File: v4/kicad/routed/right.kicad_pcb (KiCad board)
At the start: 2 copper layers, 158 x 118.6 mm, 72 parts

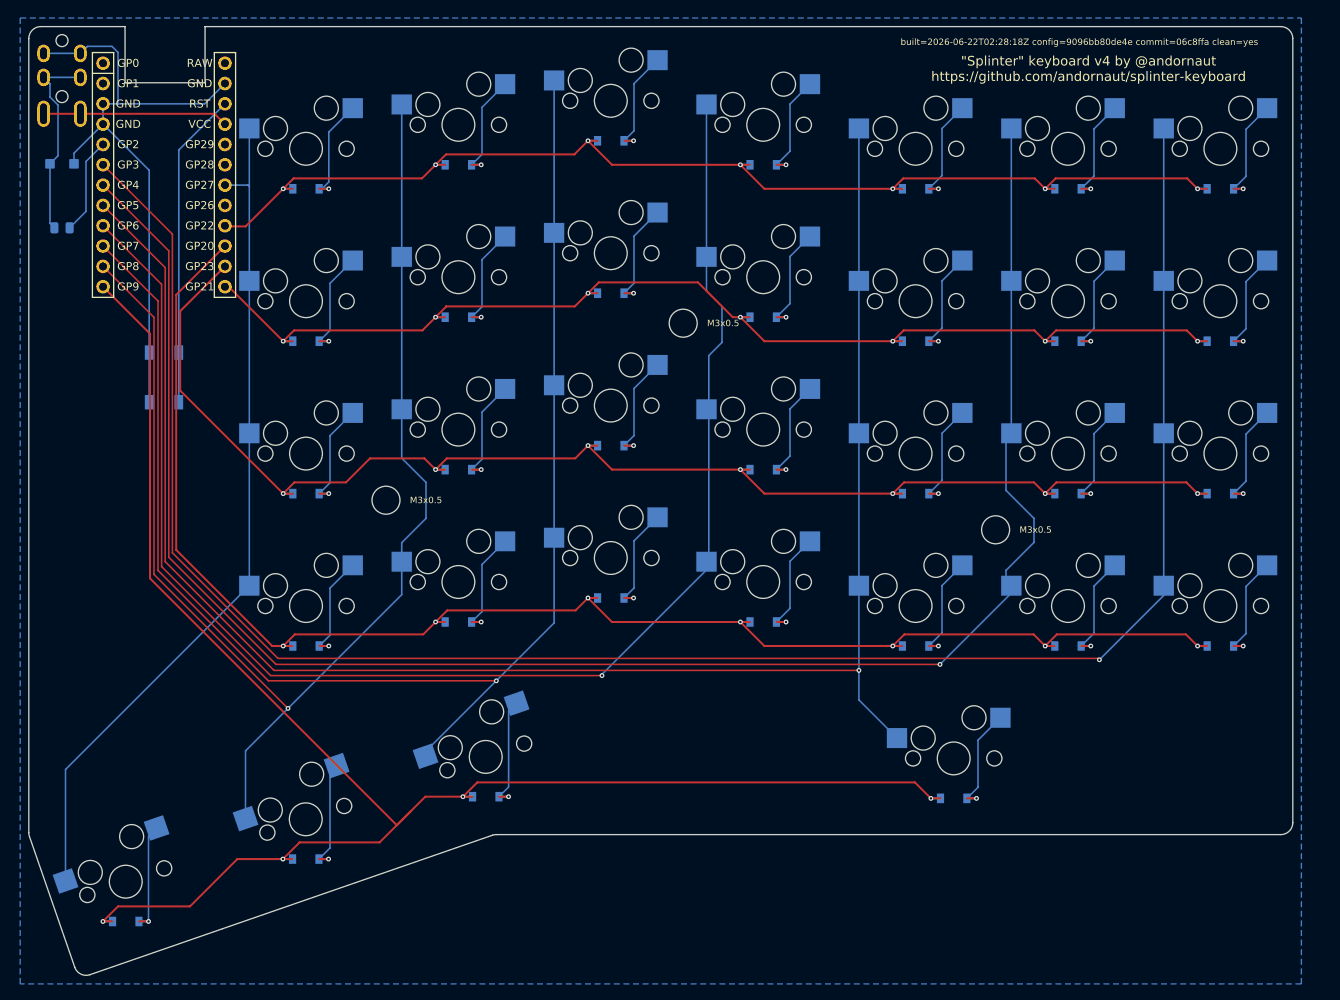
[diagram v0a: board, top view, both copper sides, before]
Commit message: v4: re-route both halves for the mirrored left-half pin mapping
Both halves are routed against the current config: the left half's matrix
nets on their MCU socket-row partners, and the MCU seated at the new mcu_y.
routed/ is re-derived from unrouted/ with the GND pour and teardrops (281
left, 296 right).

validate:provenance, validate:firmware, the fab DRC gate and validate:fab
all pass on all four boards. The routed/ .kicad_dru files land here for the
first time: apply-project-settings writes them per tier now.
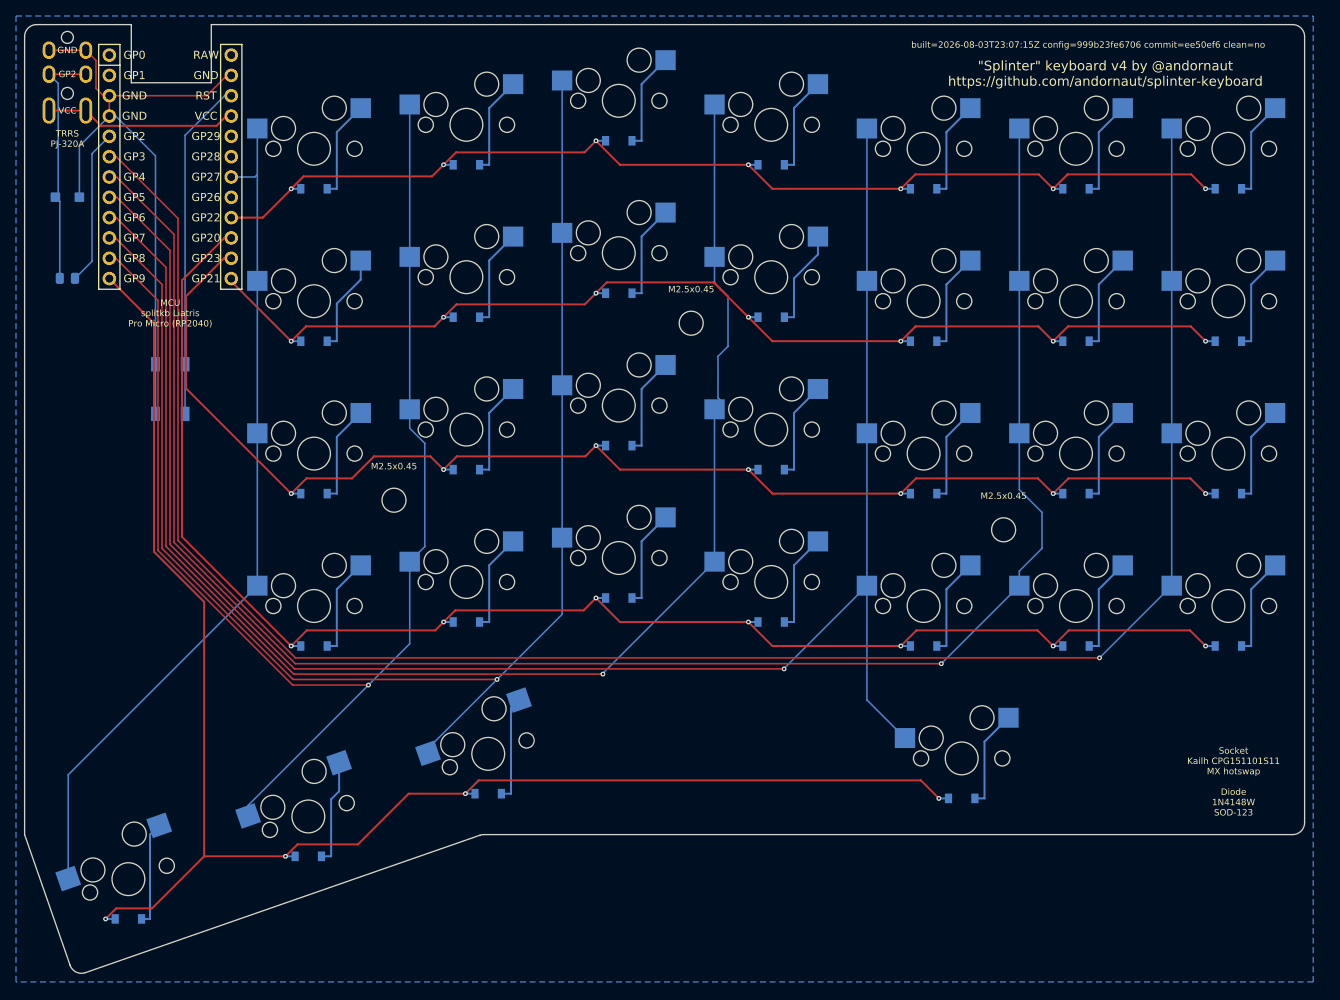
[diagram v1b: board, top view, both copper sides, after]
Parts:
- moved R1 6.35 mm to (135.7, 121.0)
- moved D33 4.22 mm to (135.7, 110.8)
- moved B1 1.66 mm to (148.5, 134.8)
- moved MCU1 1.28 mm to (148.5, 105.8)
- moved D1 1.00 mm to (223.7, 163.9)
- moved D10 1.00 mm to (185.6, 144.9)
- moved D11 1.00 mm to (185.6, 125.8)
- moved D12 1.00 mm to (185.6, 106.8)
- moved D13 1.00 mm to (166.5, 166.9)
- moved D14 1.00 mm to (166.5, 147.9)
- moved D15 1.00 mm to (166.5, 128.8)
- moved D16 1.00 mm to (166.5, 109.8)
- moved D17 1.00 mm to (247.5, 186.0)
- moved D18 1.00 mm to (242.7, 166.9)
- moved D19 1.00 mm to (242.7, 147.9)
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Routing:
- net P9: track 206.1 -> 194.2 mm
- net P15: track 147.4 -> 139.7 mm
- net P2: track 12.1 -> 19.5 mm
- net P8: track 164.7 -> 171.6 mm
- net P14: track 197.3 -> 190.6 mm
- net P10: track 149.1 -> 142.5 mm
- net DATA_RAW: track 23.9 -> 30.5 mm
- net P16: track 175.6 -> 169.9 mm
- net P5: track 218.3 -> 223.2 mm
- net GND: track 78.8 -> 82.0 mm
- net RST: track 39.7 -> 42.6 mm
- net mirror_five_num: track 15.3 -> 12.5 mm, vias 1 -> 0
- net P4: track 223.1 -> 225.0 mm
- net dash_lower: track 14.2 -> 12.5 mm, vias 1 -> 0
- net dash_upper: track 14.2 -> 12.5 mm, vias 1 -> 0
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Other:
- board size 158 x 118.6 mm -> 160 x 118.6 mm
- board text added: "GP2"
- board text added: "M2.5x0.45"
- board text added: "built=2026-08-03T23:07:15Z config=999b23fe6706 commit=ee50ef6 clean=no"
- board text removed: "DATA"
- board text removed: "M3x0.5"
- board text removed: "built=2026-06-22T02:28:18Z config=9096bb80de4e commit=06c8ffa clean=yes"

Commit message: v4: strip the copper no route uses, in the pipeline
scripts/cleanup-tracks.py deletes dangling tracks and the vias they
strand, tracks buried in a pad of their own net, tracks laid over each
other, vias duplicating a via or a plated through-hole pad, and teardrops
left decorating nothing, then merges the segments an edit split.
copy:unrouted-to-routed runs it on each master after the GND pour, so the
fab source is cleaned every build. The working boards in unrouted/ keep
that copper, since a later reroute may pick it up.

scripts/pcb_copper.py holds the point-level connectivity test the cleanup
shares with add-gnd-zone.py, which now leaves the copper about to be
stripped out of its pour-layer score.

add-keepout-zones.py: weld the Edge.Cuts gap a stripped degenerate shape
leaves. KiCad closes a sub-micron gap silently but KiKit's ring
extraction matches endpoints exactly and aborts on it. One shape is
stripped per pass, because a weld moves the endpoints of the shapes still
to be tested.

Routed masters re-synced: DRC clean, 0 unconnected items, teardrops
unchanged (281 left, 296 right).
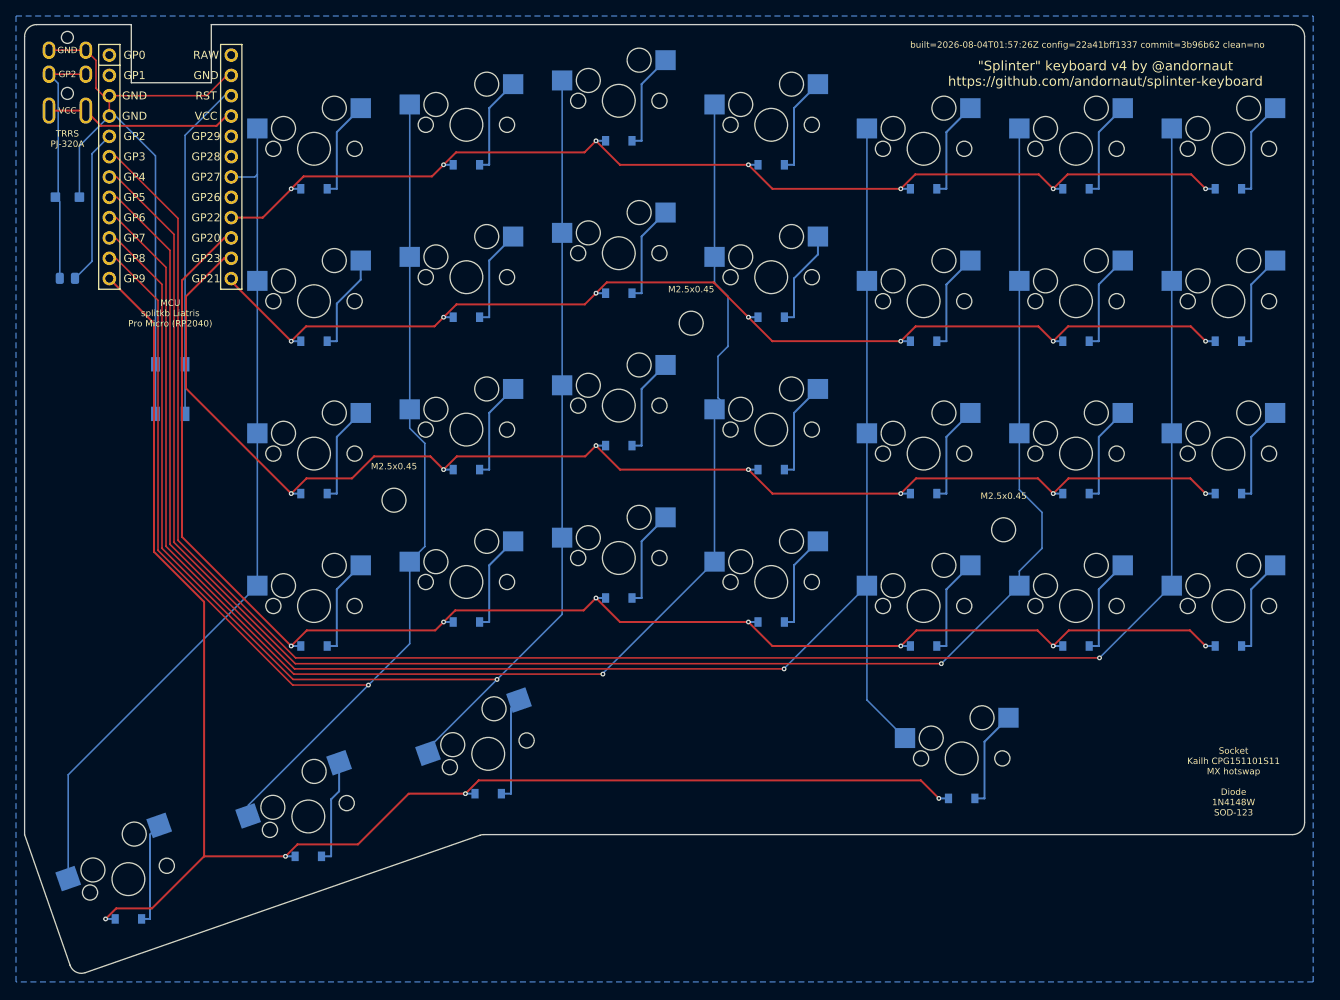
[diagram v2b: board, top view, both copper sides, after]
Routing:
- net P8: track 171.6 -> 169.5 mm
- net GND: track 82.0 -> 80.5 mm
- net mirror_three_mod: track 13.3 -> 11.9 mm
- net RST: track 42.6 -> 41.8 mm
- net P7: track 181.1 -> 180.3 mm
- net DATA_RAW: track 30.5 -> 29.7 mm
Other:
- outline, holes or cut-outs redrawn
- board text added: "built=2026-08-04T01:57:26Z config=22a41bff1337 commit=3b96b62 clean=no"
- board text removed: "built=2026-08-03T23:07:15Z config=999b23fe6706 commit=ee50ef6 clean=no"

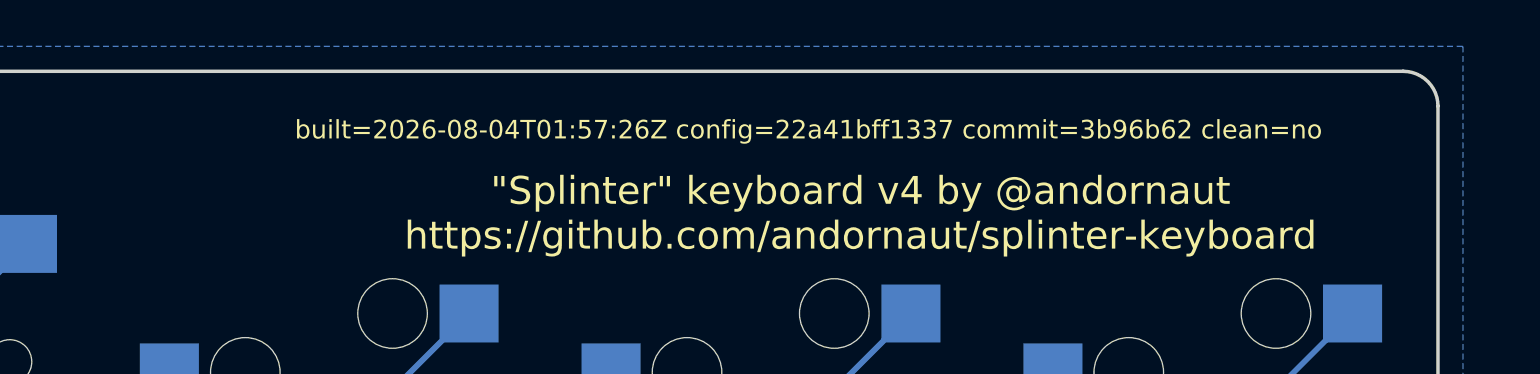
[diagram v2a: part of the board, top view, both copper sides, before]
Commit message: v4: rebuild the boards from a clean tree
Same geometry and routing; the provenance stamp now reads clean=yes
commit=ac19720, so the silkscreen and title block on the fabricated board
name the exact commit the gerbers came from.
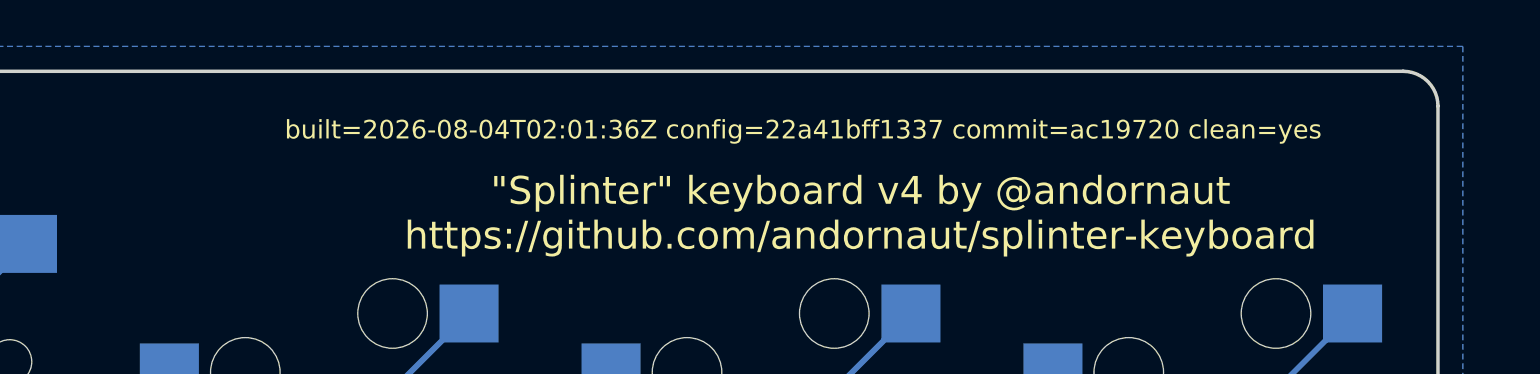
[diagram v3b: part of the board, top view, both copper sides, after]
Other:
- board text added: "built=2026-08-04T02:01:36Z config=22a41bff1337 commit=ac19720 clean=yes"
- board text removed: "built=2026-08-04T01:57:26Z config=22a41bff1337 commit=3b96b62 clean=no"

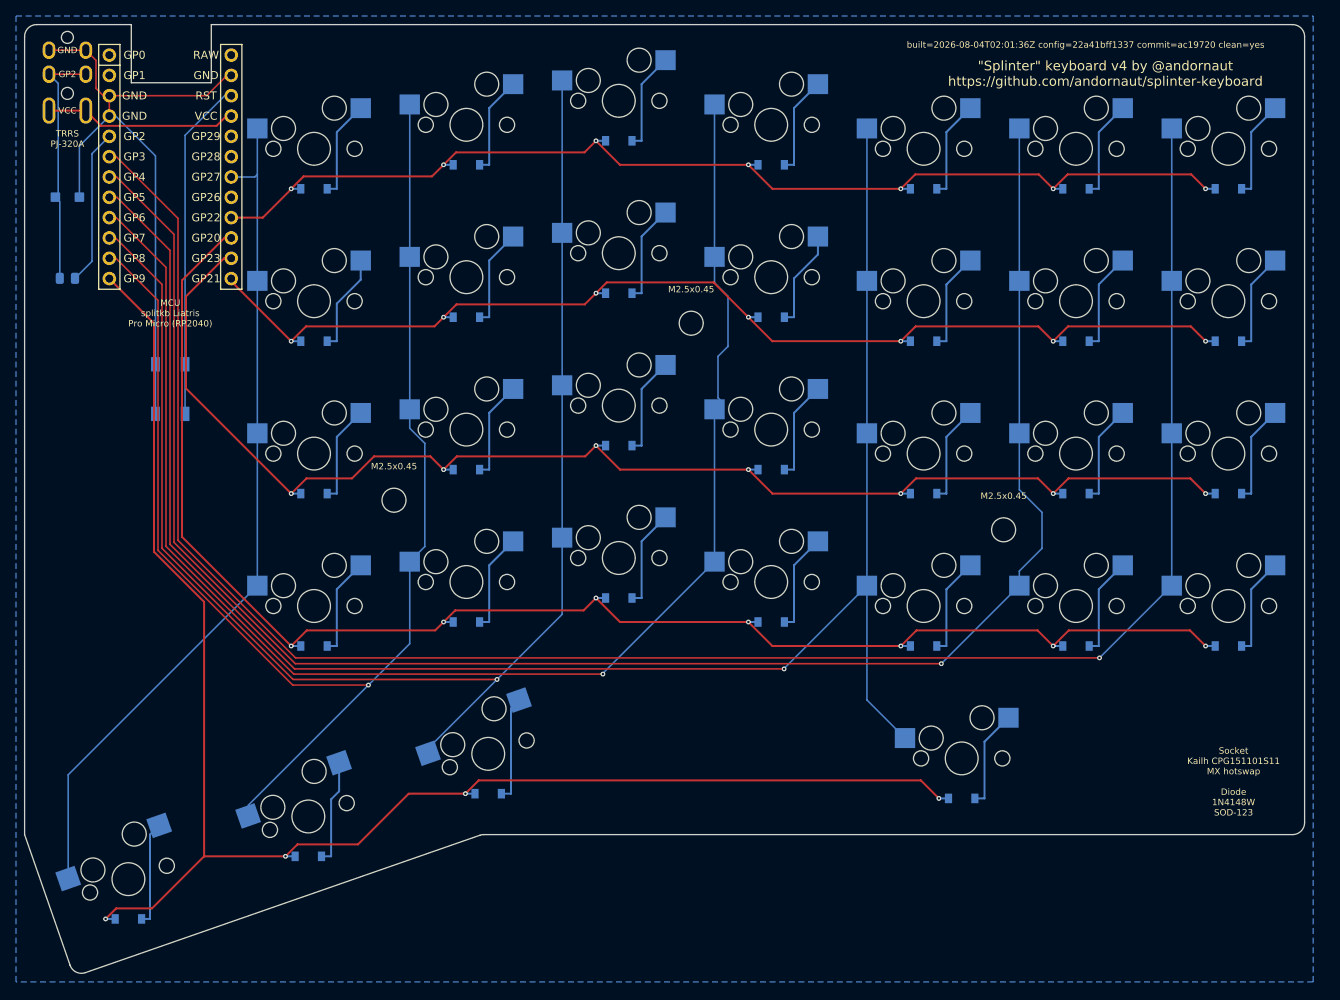
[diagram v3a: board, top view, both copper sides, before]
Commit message: v4: re-route the MCU exits, clean up to convergence
Route the header pins out straight for ~2.5mm before the first bend, so
KiCad can build a full-size teardrop instead of clipping it to a stub.
Teardrop copper is up from 296.2 to 302.1mm2 (left) and 315.2 to
323.9mm2 (right), and the count of clipped flares under 0.8mm2 is down
from 172 to 165 and 184 to 176.

cleanup-tracks.py now repeats its whole pass until one changes nothing,
capped at MAX_PASSES. The re-pour moved to the end of each pass, which
is what makes a repeat worth running: a track the old pour propped up
only reads as dangling once the pour has been re-flowed without it, and
the merge and the teardrop scan both run after the deletion fixpoint, so
nothing tested what they left. Every rule only removes copper, so a
changing pass strictly shrinks the board and the loop must converge; a
pass that still changes the board on the last allowed run is an error
and the board is left unsaved rather than half-cleaned.

Both halves converge in one changing pass. Routing is unchanged through
the pipeline round trip: 324/334 tracks, 36/38 vias, 281/297 teardrops,
0 unconnected.
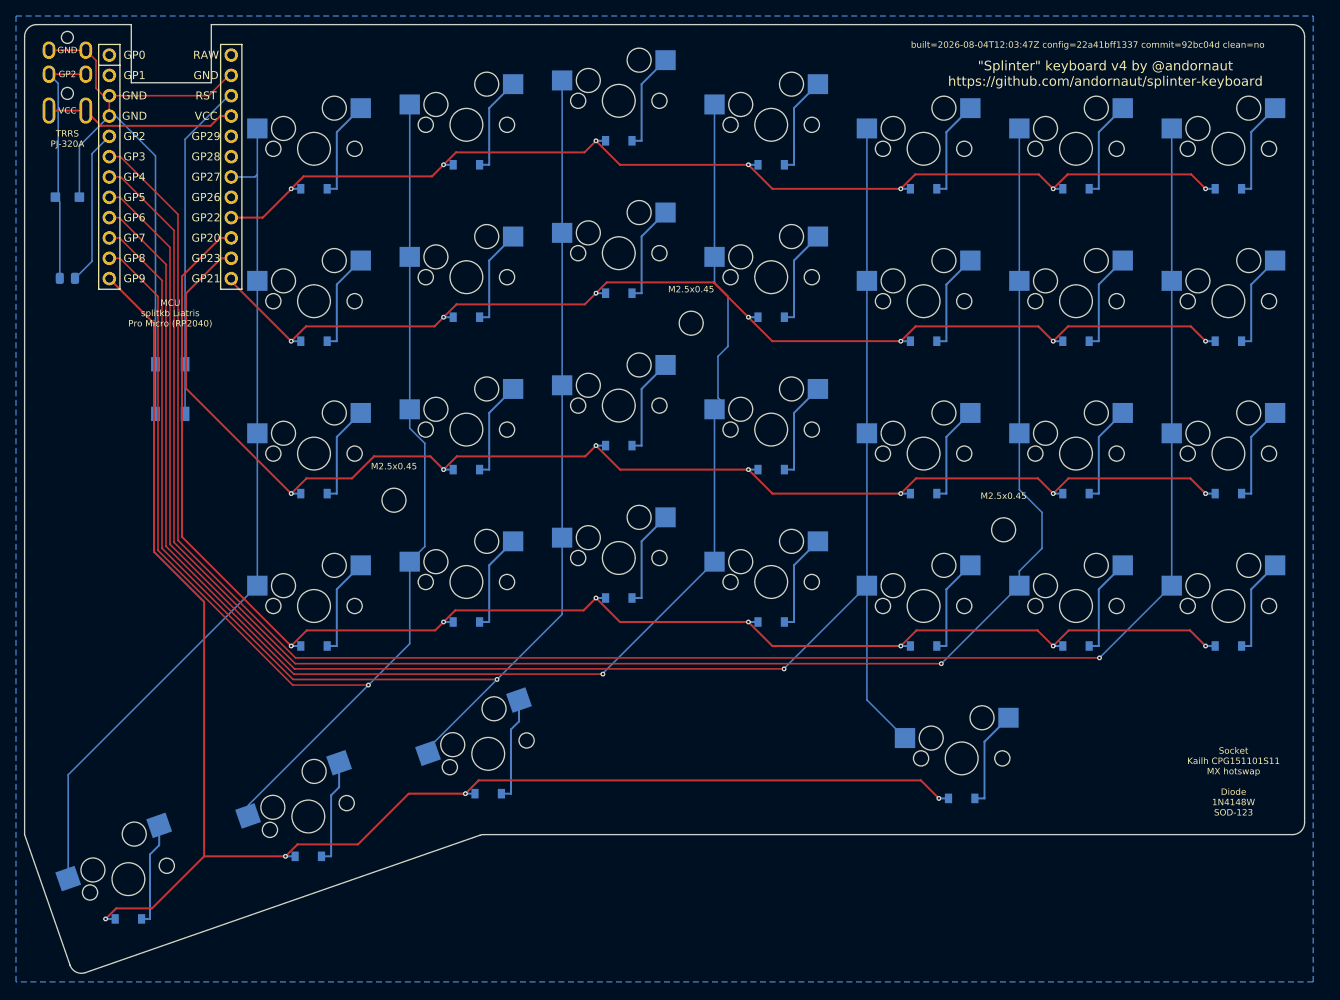
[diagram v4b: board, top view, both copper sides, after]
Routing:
- net mirror_three_mod: track 11.9 -> 13.3 mm
- net VCC: track 23.5 -> 24.1 mm
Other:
- board text added: "built=2026-08-04T12:03:47Z config=22a41bff1337 commit=92bc04d clean=no"
- board text removed: "built=2026-08-04T02:01:36Z config=22a41bff1337 commit=ac19720 clean=yes"
